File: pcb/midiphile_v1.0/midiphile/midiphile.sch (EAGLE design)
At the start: 21 parts

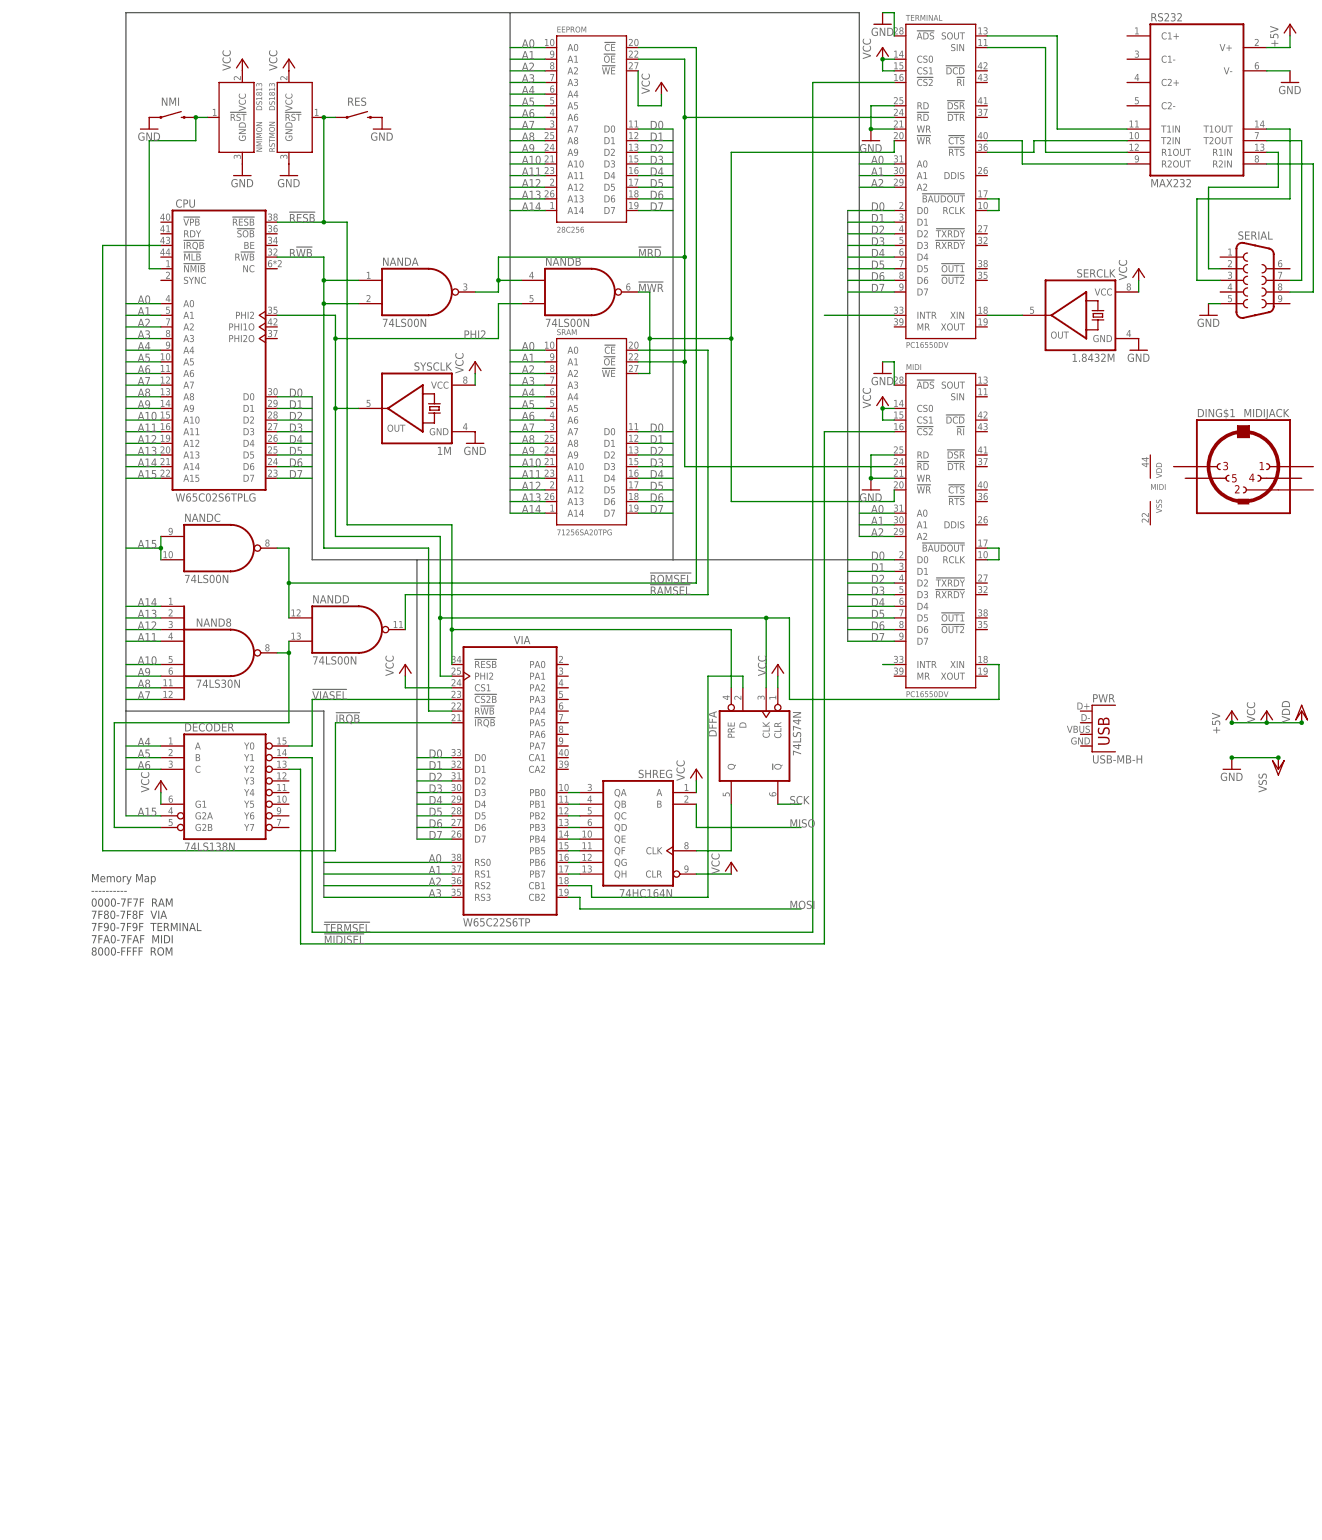
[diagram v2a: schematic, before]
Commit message: Add 16C2552, expansion headers, rectangular LEDs
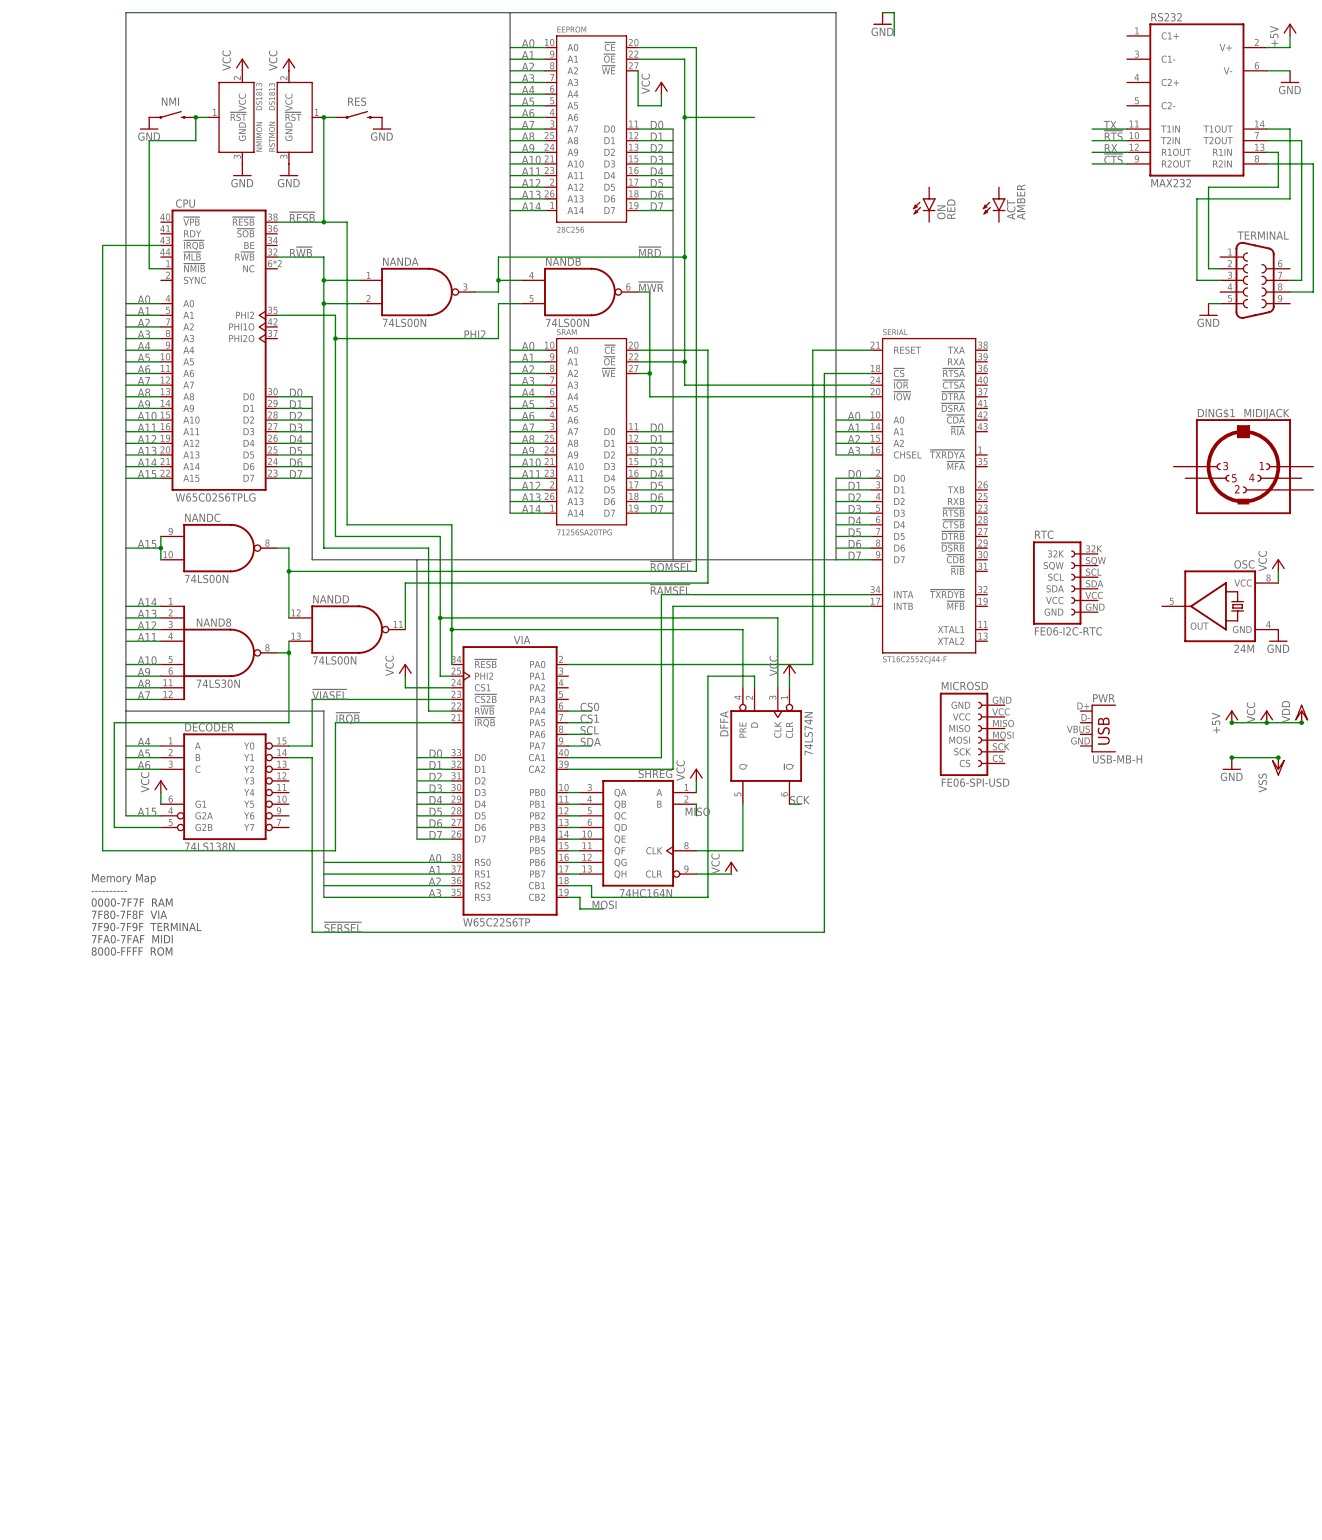
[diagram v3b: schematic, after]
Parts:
- removed MIDI: PC16550DV, 16550:PC16550DV
- removed SERCLK: 1.8432M, metal_can_oscillator:HALF_CAN_OSC
- removed SYSCLK: 1M, metal_can_oscillator:HALF_CAN_OSC
- added ACT: AMBER, led:LED_RECT_2X5MM
- added MICROSD: FE06-SPI-USD, expansion_headers:FE06-SPI-USD
- added ON: RED, led:LED_RECT_2X5MM
- added OSC: 24M, metal_can_oscillator:HALF_CAN_OSC
- added RTC: FE06-I2C-RTC, expansion_headers:FE06-I2C-RTC
- SERIAL: value (none) -> ST16C2552CJ44-F; device SparkFun-Connectors:DB9MALE -> 16550:ST16C2552CJ44-F
- TERMINAL: value PC16550DV -> (none); device 16550:PC16550DV -> SparkFun-Connectors:DB9MALE
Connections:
- removed net !MIDISEL!: DECODERA.Y2, MIDIG$1.!CS2!
- removed net !TERMSEL!: DECODERA.Y1, TERMINALG$1.!CS2!
- removed net N$16: RS232G$1.T1IN, TERMINALG$1.SOUT
- removed net N$18: RS232G$1.R1OUT, TERMINALG$1.SIN
- removed net N$19: RS232G$1.T2IN, TERMINALG$1.!RTS!
- removed net N$20: RS232G$1.R2OUT, TERMINALG$1.!CTS!
- removed net N$25: SERCLK.OUT, TERMINALG$1.XIN
- removed net N$6: TERMINALG$1.!BAUDOUT!, TERMINALG$1.RCLK
- new net !CTS!: RS232G$1.R2OUT
- new net !RTS!: RS232G$1.T2IN
- new net !SERSEL!: DECODERA.Y1, SERIALG$1.!CS!
- new net CS0: VIAVIA.PA4
- new net CS1: VIAVIA.PA5
- new net RX: RS232G$1.R1OUT
- new net SCL: VIAVIA.PA6
- new net SDA: VIAVIA.PA7
- new net TX: RS232G$1.T1IN
- net !MRD!: now also SERIALG$1.!IOR!; no longer MIDIG$1.!RD!, TERMINALG$1.!RD!
- net !MWR!: now also SERIALG$1.!IOW!; no longer MIDIG$1.!WR!, TERMINALG$1.!WR!
- net A0: now also SERIALG$1.A0; no longer MIDIG$1.A0, TERMINALG$1.A0
- net A1: now also SERIALG$1.A1; no longer MIDIG$1.A1, TERMINALG$1.A1
- net A2: now also SERIALG$1.A2; no longer MIDIG$1.A2, TERMINALG$1.A2
- net A3: now also SERIALG$1.CHSEL
- net D0: now also SERIALG$1.D0; no longer MIDIG$1.D0, TERMINALG$1.D0
- net D1: now also SERIALG$1.D1; no longer MIDIG$1.D1, TERMINALG$1.D1
- net D2: now also SERIALG$1.D2; no longer MIDIG$1.D2, TERMINALG$1.D2
- net D3: now also SERIALG$1.D3; no longer MIDIG$1.D3, TERMINALG$1.D3
- net D4: now also SERIALG$1.D4; no longer MIDIG$1.D4, TERMINALG$1.D4
- net D5: now also SERIALG$1.D5; no longer MIDIG$1.D5, TERMINALG$1.D5
- net D6: now also SERIALG$1.D6; no longer MIDIG$1.D6, TERMINALG$1.D6
- net D7: now also SERIALG$1.D7; no longer MIDIG$1.D7, TERMINALG$1.D7
- net GND: now also OSC.GND, TERMINAL.5; no longer MIDIG$1.!ADS!, MIDIG$1.RD, MIDIG$1.WR, SERCLK.GND, SERIAL.5, SYSCLK.GND, TERMINALG$1.!ADS!, TERMINALG$1.RD, TERMINALG$1.WR
- net N$21: now also TERMINAL.3; no longer SERIAL.3
- net N$22: now also TERMINAL.2; no longer SERIAL.2
- net N$23: now also TERMINAL.7; no longer SERIAL.7
- net N$24: now also TERMINAL.8; no longer SERIAL.8
- net N$3: now also SERIALG$1.INTB, VIAVIA.CA2; no longer MIDIG$1.INTR
- net N$4: now also SERIALG$1.INTA, VIAVIA.CA1; no longer TERMINALG$1.INTR
- net N$5: now also SERIALG$1.RESET, VIAVIA.PA0; no longer MIDIG$1.!BAUDOUT!, MIDIG$1.RCLK
- net PHI2: no longer MIDIG$1.XIN, SYSCLK.OUT
- net VCC: now also OSC.VCC; no longer MIDIG$1.CS0, MIDIG$1.CS1, SERCLK.VCC, SYSCLK.VCC, TERMINALG$1.CS0, TERMINALG$1.CS1
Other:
- moved on the sheet: DFFA
